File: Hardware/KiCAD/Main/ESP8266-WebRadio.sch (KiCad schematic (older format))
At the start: 45 parts, among them K1 AUDIO, K2 POWER, K3 EARPHONES, P1 UART, P2 PROG, U1 LM1117-3.3, U2 LM1117-1.8, U3 23LCV1024, U4 ESP8266_ESP-12, U5 NE5532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

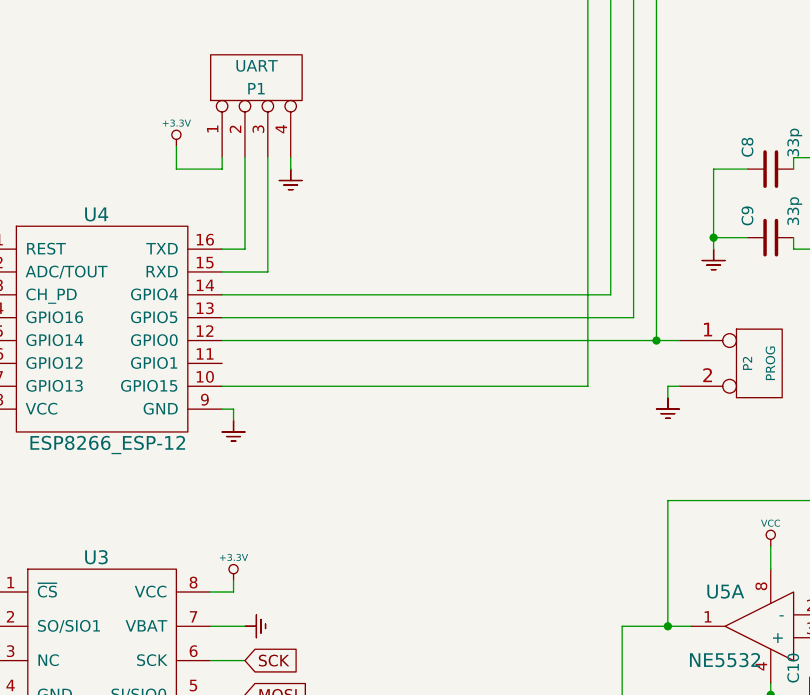
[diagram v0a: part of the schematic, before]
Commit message: Added pullups in schematic and PCB
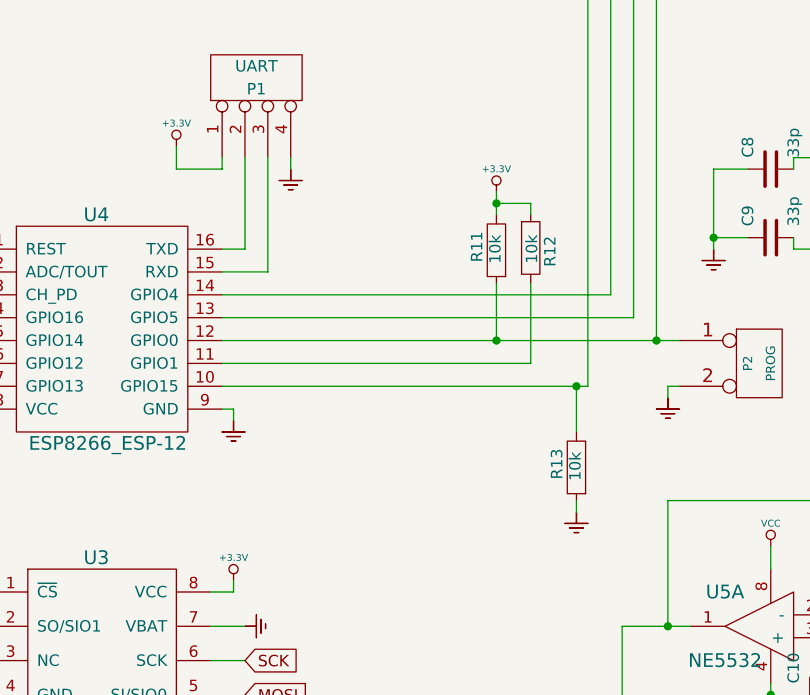
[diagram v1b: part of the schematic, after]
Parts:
- added R11, R12, R13: 10k, symbol R
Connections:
- net +3.3V: now also R11.2, R12.1
- net GND: now also R13.1
- net at U4.10 (GPIO15), U6.23 (xCS): now also R13.2
- net at U4.11 (GPIO1): now also R12.2
- net at P2.1 (P1), U4.12 (GPIO0), U6.3 (xRESET): now also R11.1
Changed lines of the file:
@@
 Sheet 1 1
 Title "ESP8266 SHOUTcast player"
-Date "16 aug 2015"
+Date "1 sep 2015"
 Rev "1.0"
 Comp "Piotr Sperka"
@@
 $EndComp
 $Comp
-L GND #PWR01
+L GND #PWR6
 U 1 1 55CF4532
 P 1650 1800
-F 0 "#PWR01" H 1650 1800 30  0001 C CNN
+F 0 "#PWR6" H 1650 1800 30  0001 C CNN
 F 1 "GND" H 1650 1730 30  0001 C CNN
 F 2 "" H 1650 1800 60  0000 C CNN
@@
 $EndComp
 $Comp
-L VCC #PWR02
+L VCC #PWR1
 U 1 1 55CF4541
 P 1050 1300
-F 0 "#PWR02" H 1050 1400 30  0001 C CNN
+F 0 "#PWR1" H 1050 1400 30  0001 C CNN
 F 1 "VCC" H 1050 1400 30  0000 C CNN
 F 2 "" H 1050 1300 60  0000 C CNN
@@
 $EndComp
 $Comp
-L +3.3V #PWR03
+L +3.3V #PWR9
 U 1 1 55CF4550
 P 2200 1300
-F 0 "#PWR03" H 2200 1260 30  0001 C CNN
+F 0 "#PWR9" H 2200 1260 30  0001 C CNN
 F 1 "+3.3V" H 2200 1400 30  0000 C CNN
 F 2 "" H 2200 1300 60  0000 C CNN
@@
 $EndComp
 $Comp
-L +1.8V #PWR04
+L +1.8V #PWR10
 U 1 1 55CF455F
 P 2200 2100
-F 0 "#PWR04" H 2200 2240 20  0001 C CNN
+F 0 "#PWR10" H 2200 2240 20  0001 C CNN
 F 1 "+1.8V" H 2200 2210 30  0000 C CNN
 F 2 "" H 2200 2100 60  0000 C CNN
@@
 $EndComp
 $Comp
-L GND #PWR05
+L GND #PWR7
 U 1 1 55CF4580
 P 1650 2600
-F 0 "#PWR05" H 1650 2600 30  0001 C CNN
+F 0 "#PWR7" H 1650 2600 30  0001 C CNN
 F 1 "GND" H 1650 2530 30  0001 C CNN
 F 2 "" H 1650 2600 60  0000 C CNN
@@
 $EndComp
 $Comp
-L GND #PWR06
+L GND #PWR37
 U 1 1 55CF50C2
 P 9350 2750
-F 0 "#PWR06" H 9350 2750 30  0001 C CNN
+F 0 "#PWR37" H 9350 2750 30  0001 C CNN
 F 1 "GND" H 9350 2680 30  0001 C CNN
 F 2 "" H 9350 2750 60  0000 C CNN
@@
 $EndComp
 $Comp
-L GND #PWR07
+L GND #PWR36
 U 1 1 55CF50C8
 P 8950 1150
-F 0 "#PWR07" H 8950 1150 30  0001 C CNN
+F 0 "#PWR36" H 8950 1150 30  0001 C CNN
 F 1 "GND" H 8950 1080 30  0001 C CNN
 F 2 "" H 8950 1150 60  0000 C CNN
@@
 $EndComp
 $Comp
-L GND #PWR08
+L GND #PWR30
 U 1 1 55CF50CE
 P 8400 3050
-F 0 "#PWR08" H 8400 3050 30  0001 C CNN
+F 0 "#PWR30" H 8400 3050 30  0001 C CNN
 F 1 "GND" H 8400 2980 30  0001 C CNN
 F 2 "" H 8400 3050 60  0000 C CNN
@@
 $EndComp
 $Comp
-L GND #PWR09
+L GND #PWR31
 U 1 1 55CF50D4
 P 8400 5100
-F 0 "#PWR09" H 8400 5100 30  0001 C CNN
+F 0 "#PWR31" H 8400 5100 30  0001 C CNN
 F 1 "GND" H 8400 5030 30  0001 C CNN
 F 2 "" H 8400 5100 60  0000 C CNN
@@
 $EndComp
 $Comp
-L +1.8V #PWR010
+L +1.8V #PWR34
 U 1 1 55CF5252
 P 8750 2250
-F 0 "#PWR010" H 8750 2390 20  0001 C CNN
+F 0 "#PWR34" H 8750 2390 20  0001 C CNN
 F 1 "+1.8V" H 8750 2360 30  0000 C CNN
 F 2 "" H 8750 2250 60  0000 C CNN
@@
 $EndComp
 $Comp
-L +3.3V #PWR011
+L +3.3V #PWR33
 U 1 1 55CF55EA
 P 8600 3400
-F 0 "#PWR011" H 8600 3360 30  0001 C CNN
+F 0 "#PWR33" H 8600 3360 30  0001 C CNN
 F 1 "+3.3V" H 8600 3500 30  0000 C CNN
 F 2 "" H 8600 3400 60  0000 C CNN
@@
 $EndComp
 $Comp
-L +3.3V #PWR012
+L +3.3V #PWR32
 U 1 1 55CF565D
 P 8550 1600
-F 0 "#PWR012" H 8550 1560 30  0001 C CNN
+F 0 "#PWR32" H 8550 1560 30  0001 C CNN
 F 1 "+3.3V" H 8550 1700 30  0000 C CNN
 F 2 "" H 8550 1600 60  0000 C CNN
@@
 $EndComp
 $Comp
-L GND #PWR013
+L GND #PWR29
 U 1 1 55CF5AD2
 P 6150 5500
-F 0 "#PWR013" H 6150 5500 30  0001 C CNN
+F 0 "#PWR29" H 6150 5500 30  0001 C CNN
 F 1 "GND" H 6150 5430 30  0001 C CNN
 F 2 "" H 6150 5500 60  0000 C CNN
@@
 $EndComp
 $Comp
-L +3.3V #PWR014
+L +3.3V #PWR28
 U 1 1 55CF5F31
 P 6150 2800
-F 0 "#PWR014" H 6150 2760 30  0001 C CNN
+F 0 "#PWR28" H 6150 2760 30  0001 C CNN
 F 1 "+3.3V" H 6150 2900 30  0000 C CNN
 F 2 "" H 6150 2800 60  0000 C CNN
@@
 $EndComp
 $Comp
-L GND #PWR015
+L GND #PWR22
 U 1 1 55CF6038
 P 4900 4000
-F 0 "#PWR015" H 4900 4000 30  0001 C CNN
+F 0 "#PWR22" H 4900 4000 30  0001 C CNN
 F 1 "GND" H 4900 3930 30  0001 C CNN
 F 2 "" H 4900 4000 60  0000 C CNN
@@
 $EndComp
 $Comp
-L GND #PWR016
+L GND #PWR35
 U 1 1 55CF6AAC
 P 8900 4900
-F 0 "#PWR016" H 8900 4900 30  0001 C CNN
+F 0 "#PWR35" H 8900 4900 30  0001 C CNN
 F 1 "GND" H 8900 4830 30  0001 C CNN
 F 2 "" H 8900 4900 60  0000 C CNN
@@
 $EndComp
 $Comp
-L +3.3V #PWR017
+L +3.3V #PWR11
 U 1 1 55CF6F9B
 P 2550 3500
-F 0 "#PWR017" H 2550 3460 30  0001 C CNN
+F 0 "#PWR11" H 2550 3460 30  0001 C CNN
 F 1 "+3.3V" H 2550 3600 30  0000 C CNN
 F 2 "" H 2550 3500 60  0000 C CNN
@@
 $EndComp
 $Comp
-L GND #PWR018
+L GND #PWR15
 U 1 1 55CF6FA1
 P 3050 3650
-F 0 "#PWR018" H 3050 3650 30  0001 C CNN
+F 0 "#PWR15" H 3050 3650 30  0001 C CNN
 F 1 "GND" H 3050 3580 30  0001 C CNN
 F 2 "" H 3050 3650 60  0000 C CNN
@@
 SCK
 $Comp
-L +3.3V #PWR019
+L +3.3V #PWR4
 U 1 1 55CF76AD
 P 1300 4600
-F 0 "#PWR019" H 1300 4560 30  0001 C CNN
+F 0 "#PWR4" H 1300 4560 30  0001 C CNN
 F 1 "+3.3V" H 1300 4700 30  0000 C CNN
 F 2 "" H 1300 4600 60  0000 C CNN
@@
 $EndComp
 $Comp
-L GND #PWR020
+L GND #PWR5
 U 1 1 55CF76B9
 P 1550 5050
-F 0 "#PWR020" H 1550 5050 30  0001 C CNN
+F 0 "#PWR5" H 1550 5050 30  0001 C CNN
 F 1 "GND" H 1550 4980 30  0001 C CNN
 F 2 "" H 1550 5050 60  0000 C CNN
@@
 $EndComp
 $Comp
-L GND #PWR021
+L GND #PWR12
 U 1 1 55CF78E7
 P 2800 4750
-F 0 "#PWR021" H 2800 4750 30  0001 C CNN
+F 0 "#PWR12" H 2800 4750 30  0001 C CNN
 F 1 "GND" H 2800 4680 30  0001 C CNN
 F 2 "" H 2800 4750 60  0000 C CNN
@@
 $EndComp
 $Comp
-L +3.3V #PWR022
+L +3.3V #PWR3
 U 1 1 55CF7E3D
 P 1200 4100
-F 0 "#PWR022" H 1200 4060 30  0001 C CNN
+F 0 "#PWR3" H 1200 4060 30  0001 C CNN
 F 1 "+3.3V" H 1200 4200 30  0000 C CNN
 F 2 "" H 1200 4100 60  0000 C CNN
@@
 $EndComp
 $Comp
-L GND #PWR023
+L GND #PWR21
 U 1 1 55CF80BB
 P 4700 4650
-F 0 "#PWR023" H 4700 4650 30  0001 C CNN
+F 0 "#PWR21" H 4700 4650 30  0001 C CNN
 F 1 "GND" H 4700 4580 30  0001 C CNN
 F 2 "" H 4700 4650 60  0000 C CNN
@@
 $EndComp
 $Comp
-L GND #PWR024
+L GND #PWR8
 U 1 1 55CF8532
 P 1650 6000
-F 0 "#PWR024" H 1650 6000 30  0001 C CNN
+F 0 "#PWR8" H 1650 6000 30  0001 C CNN
 F 1 "GND" H 1650 5930 30  0001 C CNN
 F 2 "" H 1650 6000 60  0000 C CNN
@@
 $EndComp
 $Comp
-L +3.3V #PWR025
+L +3.3V #PWR13
 U 1 1 55CF8538
 P 2800 5400
-F 0 "#PWR025" H 2800 5360 30  0001 C CNN
+F 0 "#PWR13" H 2800 5360 30  0001 C CNN
 F 1 "+3.3V" H 2800 5500 30  0000 C CNN
 F 2 "" H 2800 5400 60  0000 C CNN
@@
 $EndComp
 $Comp
-L GND #PWR026
+L GND #PWR14
 U 1 1 55CF860A
 P 2900 5600
-F 0 "#PWR026" H 2900 5600 30  0001 C CNN
+F 0 "#PWR14" H 2900 5600 30  0001 C CNN
 F 1 "GND" H 2900 5530 30  0001 C CNN
 F 2 "" H 2900 5600 60  0000 C CNN
@@
 $EndComp
 $Comp
-L VCC #PWR027
+L VCC #PWR17
 U 1 1 55CF9068
 P 3950 1050
-F 0 "#PWR027" H 3950 1150 30  0001 C CNN
+F 0 "#PWR17" H 3950 1150 30  0001 C CNN
 F 1 "VCC" H 3950 1150 30  0000 C CNN
 F 2 "" H 3950 1050 60  0000 C CNN
@@
 $EndComp
 $Comp
-L GND #PWR028
+L GND #PWR16
 U 1 1 55CF906E
 P 3700 1500
-F 0 "#PWR028" H 3700 1500 30  0001 C CNN
+F 0 "#PWR16" H 3700 1500 30  0001 C CNN
 F 1 "GND" H 3700 1430 30  0001 C CNN
 F 2 "" H 3700 1500 60  0000 C CNN
@@
 $EndComp
 $Comp
-L -6V #PWR22
+L -6V #PWR24
 U 1 1 55CF971C
 P 5150 5950
-F 0 "#PWR22" H 5150 6070 20  0001 C CNN
+F 0 "#PWR24" H 5150 6070 20  0001 C CNN
 F 1 "-VCC" H 5150 6050 20  0000 C CNN
 F 2 "" H 5150 5950 60  0000 C CNN
@@
 $EndComp
 $Comp
-L -6V #PWR24
+L -6V #PWR26
 U 1 1 55CF9722
 P 5150 6950
-F 0 "#PWR24" H 5150 7070 20  0001 C CNN
+F 0 "#PWR26" H 5150 7070 20  0001 C CNN
 F 1 "-VCC" H 5150 7050 20  0000 C CNN
 F 2 "" H 5150 6950 60  0000 C CNN
@@
 $EndComp
 $Comp
-L VCC #PWR029
+L VCC #PWR25
 U 1 1 55CF9728
 P 5150 6250
-F 0 "#PWR029" H 5150 6350 30  0001 C CNN
+F 0 "#PWR25" H 5150 6350 30  0001 C CNN
 F 1 "VCC" H 5150 6350 30  0000 C CNN
 F 2 "" H 5150 6250 60  0000 C CNN
@@
 $EndComp
 $Comp
-L VCC #PWR030
+L VCC #PWR23
 U 1 1 55CF9758
 P 5150 5250
-F 0 "#PWR030" H 5150 5350 30  0001 C CNN
+F 0 "#PWR23" H 5150 5350 30  0001 C CNN
 F 1 "VCC" H 5150 5350 30  0000 C CNN
 F 2 "" H 5150 5250 60  0000 C CNN
@@
 $EndComp
 $Comp
-L GND #PWR031
+L GND #PWR27
 U 1 1 55CFB582
 P 5900 6200
-F 0 "#PWR031" H 5900 6200 30  0001 C CNN
+F 0 "#PWR27" H 5900 6200 30  0001 C CNN
 F 1 "GND" H 5900 6130 30  0001 C CNN
 F 2 "" H 5900 6200 60  0000 C CNN
@@
 	5950 5050 5950 5100
 $Comp
-L +3.3V #PWR032
+L +3.3V #PWR2
 U 1 1 55CF9342
 P 1050 2150
-F 0 "#PWR032" H 1050 2110 30  0001 C CNN
+F 0 "#PWR2" H 1050 2110 30  0001 C CNN
 F 1 "+3.3V" H 1050 2250 30  0000 C CNN
 F 2 "" H 1050 2150 60  0000 C CNN
@@
 Wire Wire Line
 	8950 1250 8750 1250
+$Comp
+L R R12
+U 1 1 55E5CB71
+P 4100 3950
+F 0 "R12" V 4185 3940 50  0000 C CNN
+F 1 "10k" V 4105 3950 50  0000 C CNN
+F 2 "" H 4100 3950 60  0000 C CNN
+F 3 "" H 4100 3950 60  0000 C CNN
+	1    4100 3950
+	1    0    0    -1
+$EndComp
+$Comp
+L R R13
+U 1 1 55E5CB77
+P 4300 4900
+F 0 "R13" V 4385 4890 50  0000 C CNN
+F 1 "10k" V 4305 4900 50  0000 C CNN
+F 2 "" H 4300 4900 60  0000 C CNN
+F 3 "" H 4300 4900 60  0000 C CNN
+	1    4300 4900
+	-1   0    0    1
+$EndComp
+$Comp
+L R R11
+U 1 1 55E5CB7D
+P 3950 3950
+F 0 "R11" V 4035 3940 50  0000 C CNN
+F 1 "10k" V 3955 3950 50  0000 C CNN
+F 2 "" H 3950 3950 60  0000 C CNN
+F 3 "" H 3950 3950 60  0000 C CNN
+	1    3950 3950
+	-1   0    0    1
+$EndComp
+Wire Wire Line
+	2750 4450 4100 4450
+Wire Wire Line
+	4300 4750 4300 4550
+Connection ~ 4300 4550
+$Comp
+L GND #PWR20
+U 1 1 55E5D205
+P 4300 5150
+F 0 "#PWR20" H 4300 5150 30  0001 C CNN
+F 1 "GND" H 4300 5080 30  0001 C CNN
+F 2 "" H 4300 5150 60  0000 C CNN
+F 3 "" H 4300 5150 60  0000 C CNN
+	1    4300 5150
+	1    0    0    -1
+$EndComp
+Wire Wire Line
+	4300 5100 4300 5050
+Wire Wire Line
+	4100 4450 4100 4100
+Wire Wire Line
+	3950 4100 3950 4350
+Connection ~ 3950 4350
+$Comp
+L +3.3V #PWR19
+U 1 1 55E5D535
+P 3950 3700
+F 0 "#PWR19" H 3950 3660 30  0001 C CNN
+F 1 "+3.3V" H 3950 3800 30  0000 C CNN
+F 2 "" H 3950 3700 60  0000 C CNN
+F 3 "" H 3950 3700 60  0000 C CNN
+	1    3950 3700
+	1    0    0    -1
+$EndComp
+Wire Wire Line
+	3950 3800 3950 3700
+Wire Wire Line
+	3950 3750 4100 3750
+Wire Wire Line
+	4100 3750 4100 3800
+Connection ~ 3950 3750
 $EndSCHEMATC
